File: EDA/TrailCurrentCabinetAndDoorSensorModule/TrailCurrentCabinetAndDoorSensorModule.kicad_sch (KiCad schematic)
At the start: 12 parts, among them J1 DHT22, U1 Amazon Buck Converter, U2 ESP32-C6-Super-Mini, U3 SN65HVD230, U4 ZX-XH2.54-4PWT

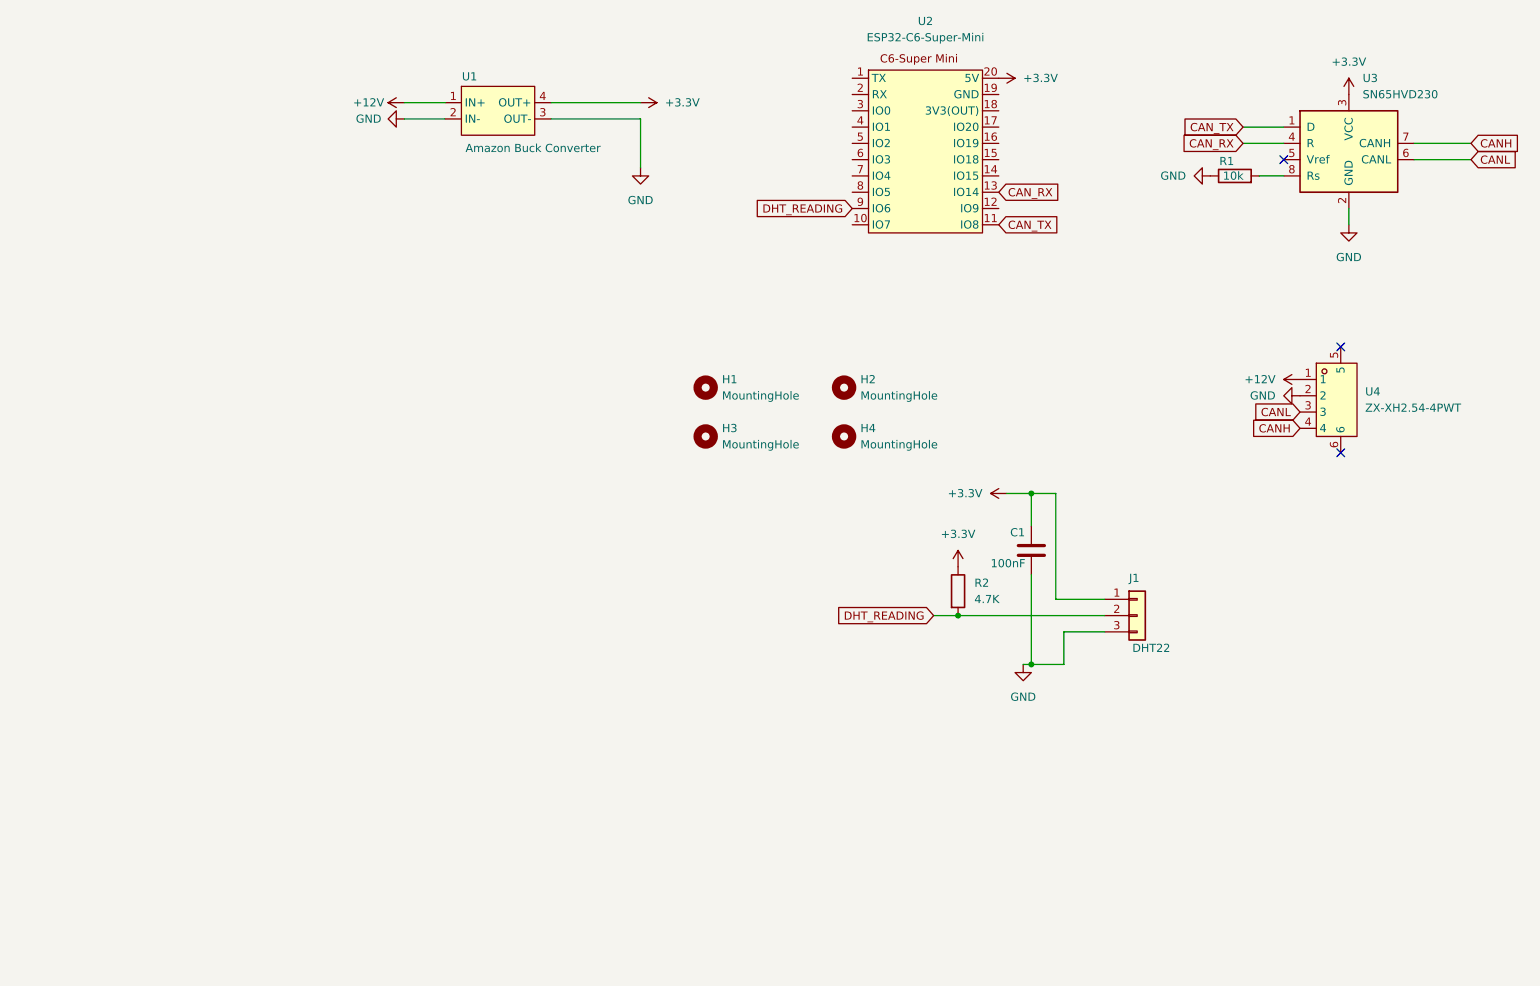
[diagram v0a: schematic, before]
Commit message: Firmware added. Schematic added. CAD files started.
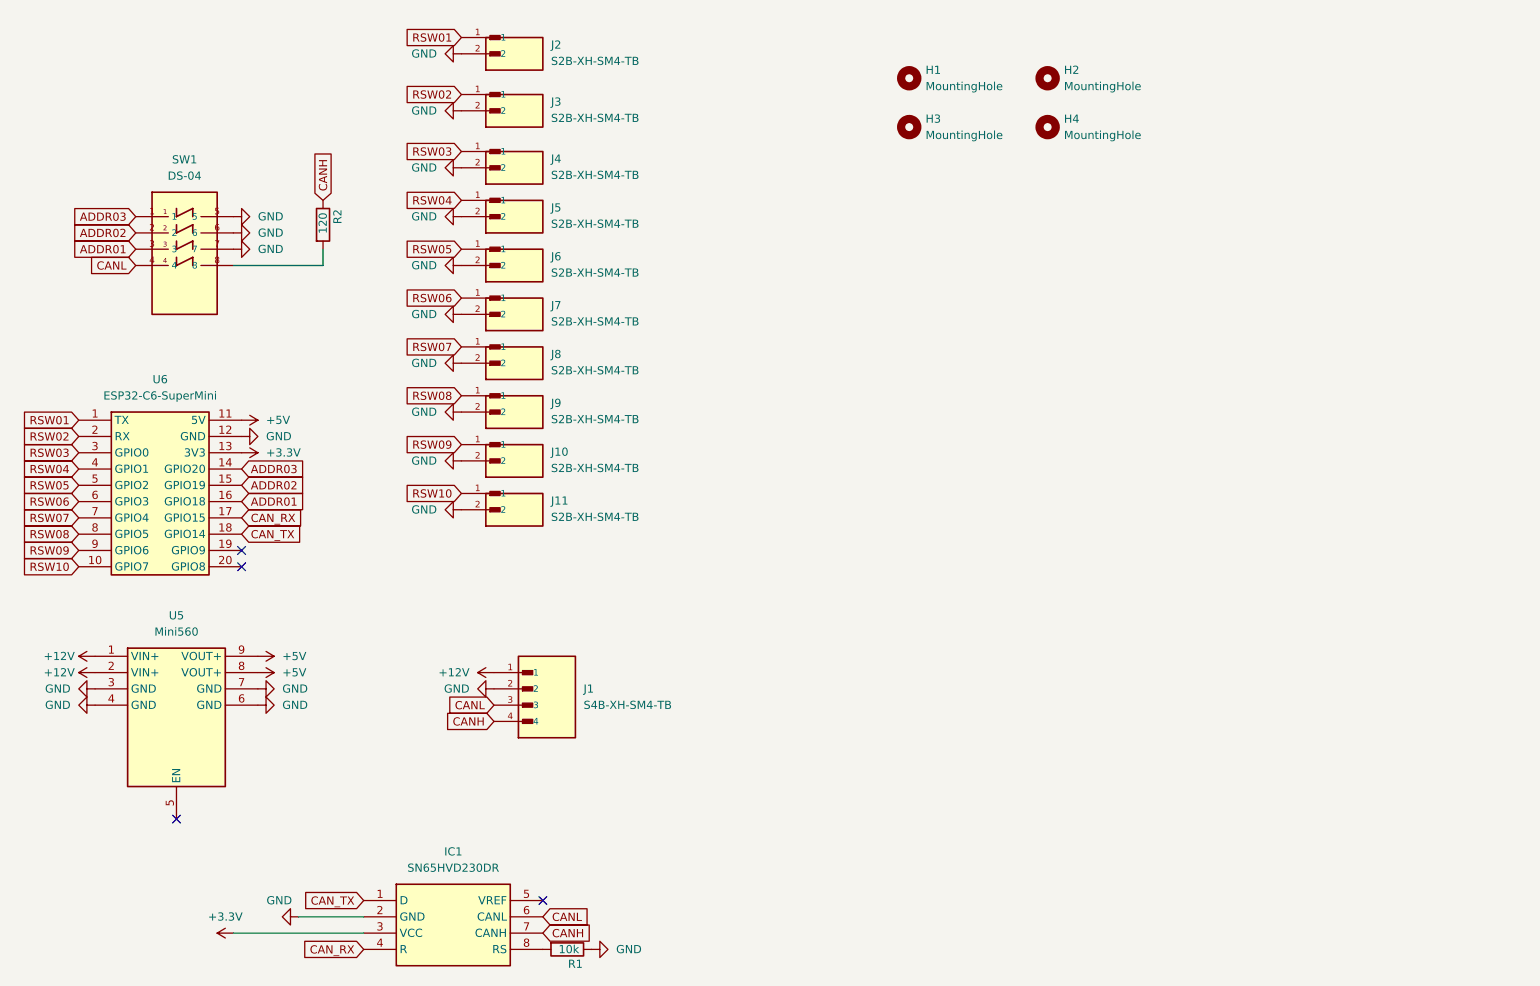
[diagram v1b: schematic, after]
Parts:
- removed C1: 100nF, Capacitor_SMD:C_1206_3216Metric_Pad1.33x1.80mm_HandSolder, symbol Device:C
- removed J1: DHT22, Connector_PinHeader_2.54mm:PinHeader_1x03_P2.54mm_Vertical, symbol Connector_Generic:Conn_01x03
- removed U1: Amazon Buck Converter, Converter_DCDC:AmazonBuckConverter, symbol Regulator_Switching:AmazonBuckConverter
- removed U2: ESP32-C6-Super-Mini, RF_Module:ESP32-C6-Super-Mini, symbol RF_Module:ESP32-C6-Super-Mini
- removed U3: SN65HVD230, Package_SO:SOIC-8_3.9x4.9mm_P1.27mm, symbol Interface_CAN_LIN:SN65HVD230
- removed U4: ZX-XH2.54-4PWT, easyeda2kicad:CONN-SMD_4P-P2.50-WAFER-254W-4P, symbol LCSC:ZX-XH2.54-4PWT
- added IC1: SN65HVD230DR, TrailCurrentFootprints:SN65HVD230DR, symbol TrailCurrentSymbolLibrary:SN65HVD230DR
- added J1: S4B-XH-SM4-TB, TrailCurrentFootprints:JST_S4B-XH-SM4-TB, symbol TrailCurrentSymbolLibrary:S4B-XH-SM4-TB
- added J10, J11, J2, J3, J4, J5, J6, J7, J8, J9: S2B-XH-SM4-TB, TrailCurrentFootprints:JST_S2B-XH-SM4-TB, symbol TrailCurrentSymbolLibrary:S2B-XH-SM4-TB
- added SW1: DS-04, TrailCurrentFootprints:DS-04, symbol TrailCurrentSymbolLibrary:DS-04
- added U5: Mini560, TrailCurrentFootprints:Mini560, symbol TrailCurrentSymbolLibrary:Mini560
- added U6: ESP32-C6-SuperMini, TrailCurrentFootprints:ESP32-C6-SuperMini_SMD, symbol TrailCurrentSymbolLibrary:ESP32-C6-SuperMini
- R2: value 4.7K -> 120; footprint Capacitor_SMD:C_1206_3216Metric_Pad1.33x1.80mm_HandSolder -> Resistor_SMD:R_1206_3216Metric_Pad1.30x1.75mm_HandSolder
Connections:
- net +12V: now also J1.1, U5.1 (VIN+), U5.2 (VIN+)
- net +3.3V: now also IC1.3 (VCC), U6.13 (3V3); no longer R2.1
- net CANH: now also R2.1, IC1.7 (CANH), J1.4
- net CANL: now also IC1.6 (CANL), J1.3, SW1.4
- net CAN_RX: now also IC1.4 (R), U6.17 (GPIO15)
- net CAN_TX: now also IC1.1 (D), U6.18 (GPIO14)
- net GND: now also IC1.2 (GND), J1.2, J10.2, J11.2, J2.2, J3.2, J4.2, J5.2, J6.2, J7.2, J8.2, J9.2, SW1.5, SW1.6, SW1.7, U5.3 (GND), U5.4 (GND), U5.6 (GND), U5.7 (GND), U6.12 (GND)
- net at R1.2: now also IC1.8 (RS)
- net DHT_READING: no longer names the net of R2.2
- net DHT_READING: now also SW1.8
- new net +5V: U5.8 (VOUT+), U5.9 (VOUT+), U6.11 (5V)
- new net ADDR01: SW1.3, U6.16 (GPIO18)
- new net ADDR02: SW1.2, U6.15 (GPIO19)
- new net ADDR03: SW1.1, U6.14 (GPIO20)
- new net RSW01: J2.1, U6.1 (TX)
- new net RSW02: J3.1, U6.2 (RX)
- new net RSW03: J4.1, U6.3 (GPIO0)
- new net RSW04: J5.1, U6.4 (GPIO1)
- new net RSW05: J6.1, U6.5 (GPIO2)
- new net RSW06: J7.1, U6.6 (GPIO3)
- new net RSW07: J8.1, U6.7 (GPIO4)
- new net RSW08: J9.1, U6.8 (GPIO5)
- new net RSW09: J10.1, U6.9 (GPIO6)
- new net RSW10: J11.1, U6.10 (GPIO7)
- no-connect marks 3 -> 4
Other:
- moved on the sheet: H1, H2, H3, H4, R1
